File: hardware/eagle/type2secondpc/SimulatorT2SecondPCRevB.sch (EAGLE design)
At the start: 5 parts

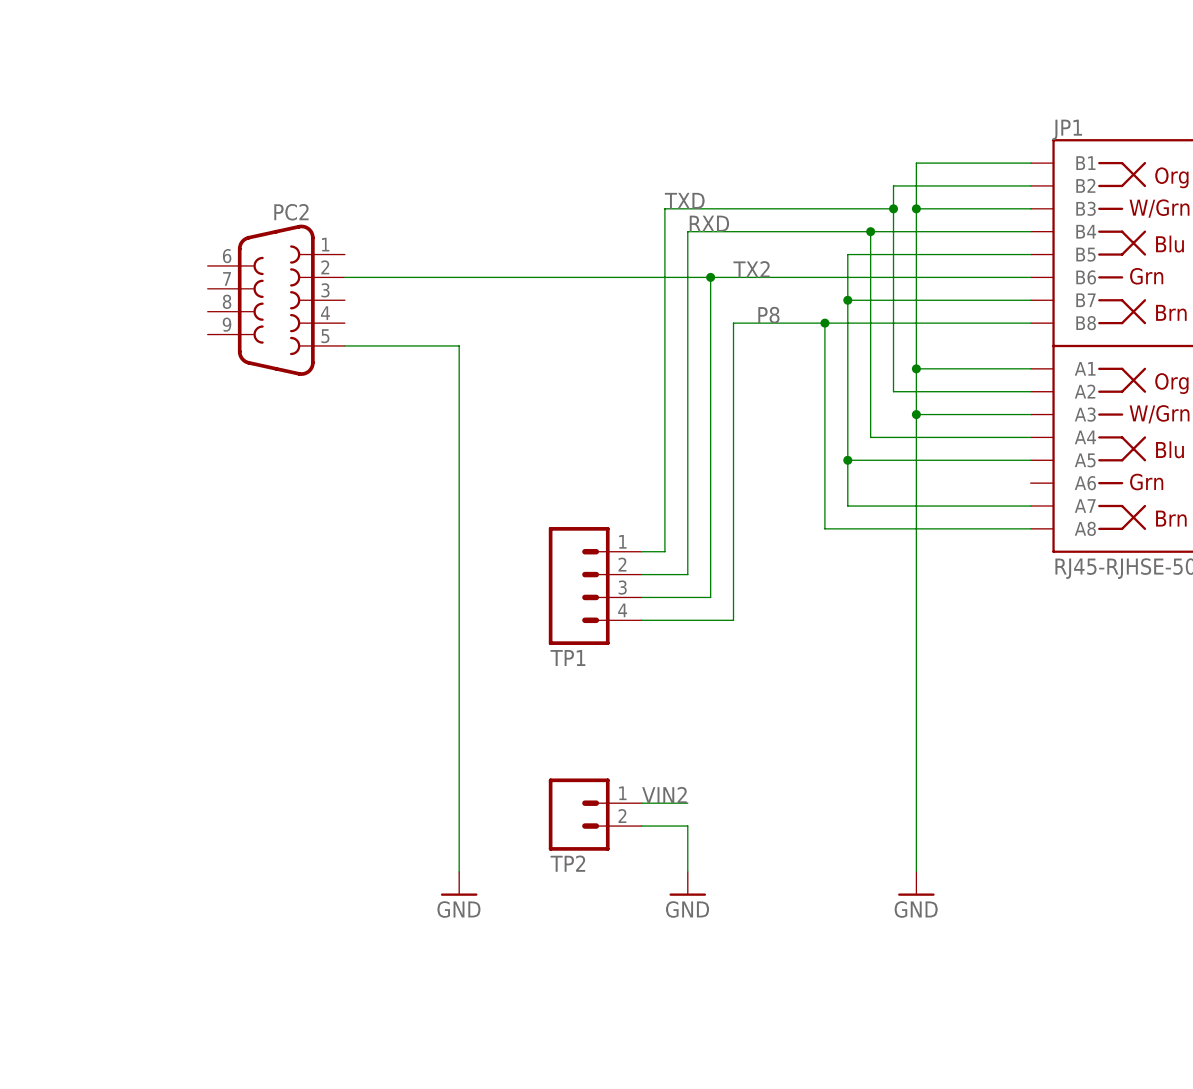
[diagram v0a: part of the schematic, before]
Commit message: Enhanced surge protection
Power Rev D, 2nd PC Rev B boards with improved surge protection,
Gerbers, Cost Estimation tool, New enclosure drilling templates.
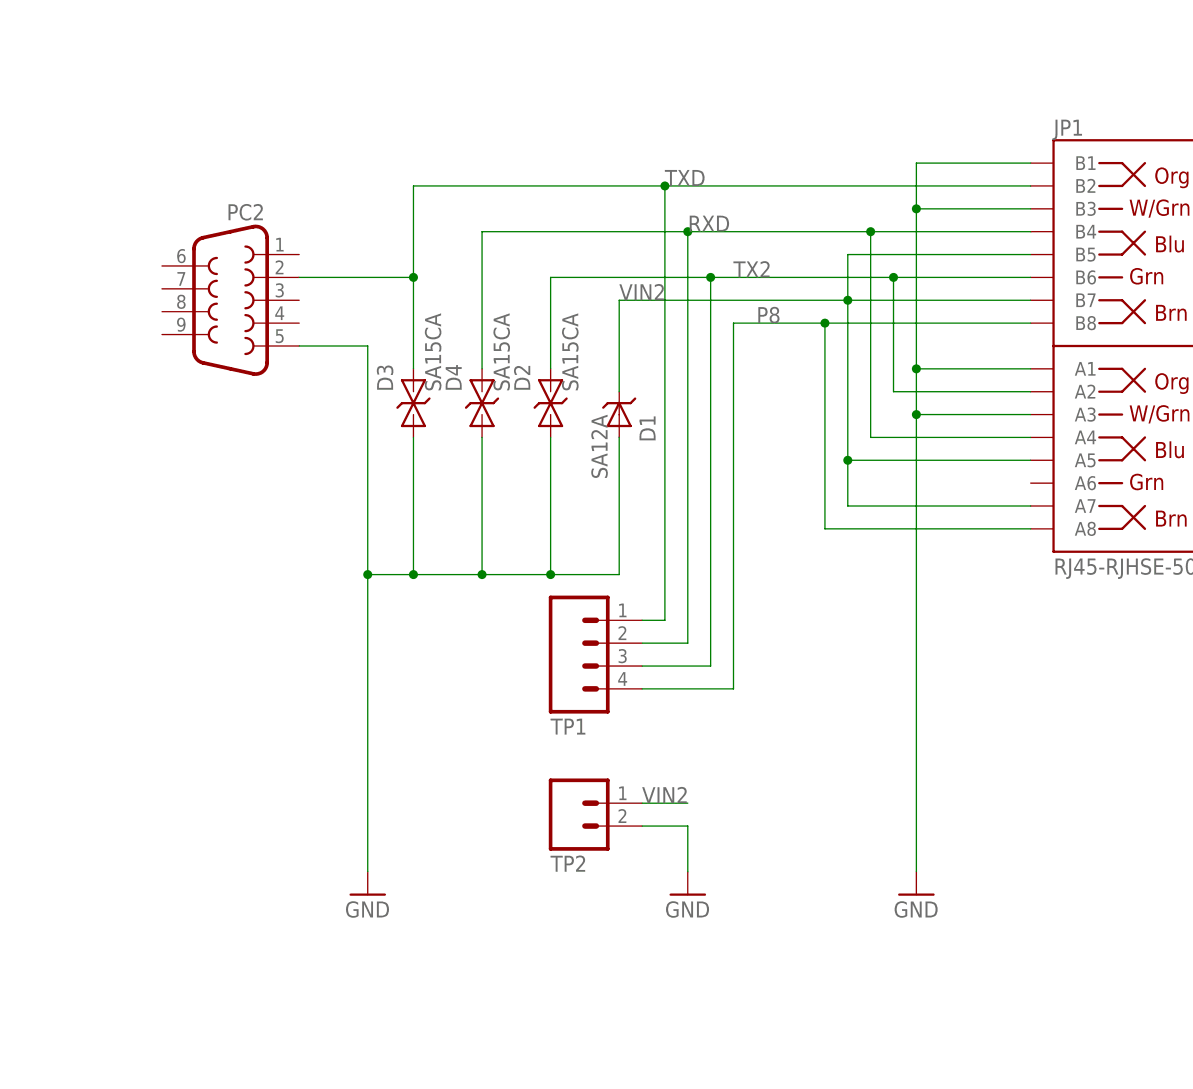
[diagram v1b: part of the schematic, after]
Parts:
- added D1: SA12A, AIC_Custom:SA12A
- added D2, D3, D4: SA15CA, AIC_Custom:SA15CA
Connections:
- net GND: now also D1.ANODE, D2.A, D3.A, D4.A
- net RXD: now also D4.C
- net TX2: now also D2.C, JP1.A2; no longer PC2.2
- net TXD: now also D3.C, PC2.2; no longer JP1.A2
- net VIN2: now also D1.CATHODE
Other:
- moved on the sheet: PC2, TP1
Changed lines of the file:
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@@
 <part name="FRAME1" library="SparkFun-Aesthetics" deviceset="FRAME-A4L" device="">
 <attribute name="CNAME" value="Simulator Type 2 Second PC"/>
-<attribute name="CREVISION" value="Rev A 04/2019"/>
+<attribute name="CREVISION" value="Rev B 07/2019"/>
 <attribute name="DESIGNER" value="A J Instone-Cowie"/>
 </part>
@@
 <part name="GND4" library="SparkFun-Aesthetics" deviceset="GND" device=""/>
 <part name="JP1" library="AIC_Custom" deviceset="RJ45-RJHSE-5080-02" device="2HOLE" value="RJ45-RJHSE-5080-022HOLE"/>
+<part name="D2" library="AIC_Custom" deviceset="SA15CA" device=""/>
+<part name="D4" library="AIC_Custom" deviceset="SA15CA" device=""/>
+<part name="D3" library="AIC_Custom" deviceset="SA15CA" device=""/>
+<part name="D1" library="AIC_Custom" deviceset="SA12A" device=""/>
 </parts>
 <sheets>
@@
 <attribute name="CREVISION" x="5.08" y="5.08" size="1.778" layer="96" display="off"/>
 </instance>
-<instance part="PC2" gate="G$1" x="96.52" y="106.68" rot="MR0"/>
+<instance part="PC2" gate="G$1" x="91.44" y="106.68" rot="MR0"/>
 <instance part="GND1" gate="1" x="167.64" y="40.64"/>
-<instance part="GND3" gate="1" x="116.84" y="40.64"/>
+<instance part="GND3" gate="1" x="106.68" y="40.64"/>
 <instance part="LOGO1" gate="G$1" x="261.62" y="175.26"/>
-<instance part="TP1" gate="G$1" x="132.08" y="76.2" rot="MR180"/>
+<instance part="TP1" gate="G$1" x="132.08" y="68.58" rot="MR180"/>
 <instance part="TP2" gate="G$1" x="129.54" y="50.8" rot="MR180"/>
 <instance part="GND4" gate="1" x="142.24" y="40.64"/>
 <instance part="JP1" gate="G$1" x="190.5" y="101.6"/>
+<instance part="D2" gate="G$1" x="127" y="93.98" rot="R90"/>
+<instance part="D4" gate="G$1" x="119.38" y="93.98" rot="R90"/>
+<instance part="D3" gate="G$1" x="111.76" y="93.98" rot="R90"/>
+<instance part="D1" gate="G$1" x="134.62" y="96.52" rot="R270"/>
 </instances>
 <busses>
@@
 <pinref part="PC2" gate="G$1" pin="5"/>
 <pinref part="GND3" gate="1" pin="GND"/>
-<wire x1="104.14" y1="101.6" x2="116.84" y2="101.6" width="0.1524" layer="91"/>
-<wire x1="116.84" y1="101.6" x2="116.84" y2="43.18" width="0.1524" layer="91"/>
+<wire x1="99.06" y1="101.6" x2="106.68" y2="101.6" width="0.1524" layer="91"/>
+<wire x1="106.68" y1="101.6" x2="106.68" y2="76.2" width="0.1524" layer="91"/>
+<pinref part="D2" gate="G$1" pin="A"/>
+<wire x1="106.68" y1="76.2" x2="106.68" y2="43.18" width="0.1524" layer="91"/>
+<wire x1="127" y1="91.44" x2="127" y2="76.2" width="0.1524" layer="91"/>
+<wire x1="127" y1="76.2" x2="119.38" y2="76.2" width="0.1524" layer="91"/>
+<junction x="106.68" y="76.2"/>
+<pinref part="D3" gate="G$1" pin="A"/>
+<wire x1="119.38" y1="76.2" x2="111.76" y2="76.2" width="0.1524" layer="91"/>
+<wire x1="111.76" y1="76.2" x2="106.68" y2="76.2" width="0.1524" layer="91"/>
+<wire x1="111.76" y1="91.44" x2="111.76" y2="76.2" width="0.1524" layer="91"/>
+<junction x="111.76" y="76.2"/>
+<pinref part="D4" gate="G$1" pin="A"/>
+<wire x1="119.38" y1="91.44" x2="119.38" y2="76.2" width="0.1524" layer="91"/>
+<junction x="119.38" y="76.2"/>
+<pinref part="D1" gate="G$1" pin="ANODE"/>
+<wire x1="134.62" y1="91.44" x2="134.62" y2="76.2" width="0.1524" layer="91"/>
+<wire x1="134.62" y1="76.2" x2="127" y2="76.2" width="0.1524" layer="91"/>
+<junction x="127" y="76.2"/>
 </segment>
 <segment>
@@
 <segment>
 <pinref part="TP1" gate="G$1" pin="2"/>
-<wire x1="137.16" y1="76.2" x2="142.24" y2="76.2" width="0.1524" layer="91"/>
-<wire x1="142.24" y1="76.2" x2="142.24" y2="114.3" width="0.1524" layer="91"/>
+<wire x1="137.16" y1="68.58" x2="142.24" y2="68.58" width="0.1524" layer="91"/>
+<wire x1="142.24" y1="68.58" x2="142.24" y2="114.3" width="0.1524" layer="91"/>
 <pinref part="JP1" gate="G$1" pin="B4"/>
 <wire x1="142.24" y1="114.3" x2="162.56" y2="114.3" width="0.1524" layer="91"/>
@@
 <wire x1="162.56" y1="91.44" x2="180.34" y2="91.44" width="0.1524" layer="91"/>
 <label x="142.24" y="114.3" size="1.778" layer="95"/>
+<pinref part="D4" gate="G$1" pin="C"/>
+<wire x1="142.24" y1="114.3" x2="119.38" y2="114.3" width="0.1524" layer="91"/>
+<wire x1="119.38" y1="114.3" x2="119.38" y2="99.06" width="0.1524" layer="91"/>
+<junction x="142.24" y="114.3"/>
 </segment>
 </net>
 <net name="TXD" class="0">
 <segment>
-<wire x1="139.7" y1="116.84" x2="165.1" y2="116.84" width="0.1524" layer="91"/>
-<wire x1="165.1" y1="116.84" x2="165.1" y2="119.38" width="0.1524" layer="91"/>
+<wire x1="139.7" y1="119.38" x2="180.34" y2="119.38" width="0.1524" layer="91"/>
 <pinref part="TP1" gate="G$1" pin="1"/>
-<wire x1="137.16" y1="78.74" x2="139.7" y2="78.74" width="0.1524" layer="91"/>
-<wire x1="139.7" y1="78.74" x2="139.7" y2="116.84" width="0.1524" layer="91"/>
+<wire x1="137.16" y1="71.12" x2="139.7" y2="71.12" width="0.1524" layer="91"/>
+<wire x1="139.7" y1="71.12" x2="139.7" y2="119.38" width="0.1524" layer="91"/>
 <pinref part="JP1" gate="G$1" pin="B2"/>
-<wire x1="165.1" y1="119.38" x2="180.34" y2="119.38" width="0.1524" layer="91"/>
-<wire x1="165.1" y1="116.84" x2="165.1" y2="96.52" width="0.1524" layer="91"/>
-<junction x="165.1" y="116.84"/>
-<pinref part="JP1" gate="G$1" pin="A2"/>
-<wire x1="165.1" y1="96.52" x2="180.34" y2="96.52" width="0.1524" layer="91"/>
-<label x="139.7" y="116.84" size="1.778" layer="95"/>
+<label x="139.7" y="119.38" size="1.778" layer="95"/>
+<pinref part="D3" gate="G$1" pin="C"/>
+<wire x1="139.7" y1="119.38" x2="111.76" y2="119.38" width="0.1524" layer="91"/>
+<wire x1="111.76" y1="119.38" x2="111.76" y2="109.22" width="0.1524" layer="91"/>
+<junction x="139.7" y="119.38"/>
+<pinref part="PC2" gate="G$1" pin="2"/>
+<wire x1="111.76" y1="109.22" x2="111.76" y2="99.06" width="0.1524" layer="91"/>
+<wire x1="99.06" y1="109.22" x2="111.76" y2="109.22" width="0.1524" layer="91"/>
+<junction x="111.76" y="109.22"/>
 </segment>
 </net>
@@
 <segment>
 <pinref part="TP1" gate="G$1" pin="3"/>
-<wire x1="137.16" y1="73.66" x2="144.78" y2="73.66" width="0.1524" layer="91"/>
-<wire x1="144.78" y1="73.66" x2="144.78" y2="109.22" width="0.1524" layer="91"/>
+<wire x1="137.16" y1="66.04" x2="144.78" y2="66.04" width="0.1524" layer="91"/>
+<wire x1="144.78" y1="66.04" x2="144.78" y2="109.22" width="0.1524" layer="91"/>
 <pinref part="JP1" gate="G$1" pin="B6"/>
-<wire x1="144.78" y1="109.22" x2="180.34" y2="109.22" width="0.1524" layer="91"/>
-<pinref part="PC2" gate="G$1" pin="2"/>
-<wire x1="144.78" y1="109.22" x2="104.14" y2="109.22" width="0.1524" layer="91"/>
+<wire x1="144.78" y1="109.22" x2="165.1" y2="109.22" width="0.1524" layer="91"/>
+<wire x1="165.1" y1="109.22" x2="180.34" y2="109.22" width="0.1524" layer="91"/>
+<wire x1="144.78" y1="109.22" x2="127" y2="109.22" width="0.1524" layer="91"/>
 <junction x="144.78" y="109.22"/>
 <label x="147.32" y="109.22" size="1.778" layer="95"/>
+<pinref part="D2" gate="G$1" pin="C"/>
+<wire x1="127" y1="99.06" x2="127" y2="109.22" width="0.1524" layer="91"/>
+<pinref part="JP1" gate="G$1" pin="A2"/>
+<wire x1="180.34" y1="96.52" x2="165.1" y2="96.52" width="0.1524" layer="91"/>
+<wire x1="165.1" y1="96.52" x2="165.1" y2="109.22" width="0.1524" layer="91"/>
+<junction x="165.1" y="109.22"/>
 </segment>
 </net>
@@
 <segment>
 <pinref part="TP1" gate="G$1" pin="4"/>
-<wire x1="137.16" y1="71.12" x2="147.32" y2="71.12" width="0.1524" layer="91"/>
-<wire x1="147.32" y1="71.12" x2="147.32" y2="104.14" width="0.1524" layer="91"/>
+<wire x1="137.16" y1="63.5" x2="147.32" y2="63.5" width="0.1524" layer="91"/>
+<wire x1="147.32" y1="63.5" x2="147.32" y2="104.14" width="0.1524" layer="91"/>
 <pinref part="JP1" gate="G$1" pin="B8"/>
 <wire x1="147.32" y1="104.14" x2="157.48" y2="104.14" width="0.1524" layer="91"/>
@@
 <wire x1="160.02" y1="83.82" x2="160.02" y2="88.9" width="0.1524" layer="91"/>
 <junction x="160.02" y="88.9"/>
+<pinref part="D1" gate="G$1" pin="CATHODE"/>
+<wire x1="160.02" y1="106.68" x2="134.62" y2="106.68" width="0.1524" layer="91"/>
+<wire x1="134.62" y1="106.68" x2="134.62" y2="96.52" width="0.1524" layer="91"/>
+<label x="134.62" y="106.68" size="1.778" layer="95"/>
 </segment>
 <segment>
